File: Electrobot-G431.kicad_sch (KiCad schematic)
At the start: 53 parts, among them J1 Conn_XT30M, J10 Conn_01x03, J11 Conn_01x03, J12 Conn_01x04, J13 Conn_01x04, J14 Conn_01x04, J15 Conn_XT30F, J2 Conn_01x03, J3 Conn_01x03, J4 Conn_01x03, J5 Conn_01x04, J6 Conn_01x04, J7 Conn_XT30F, J8 Conn_XT30F, J9 Conn_01x03, Q1 BSP-76, U1 TSR_2-2450, U2 TSR_2-2465, U3 L293D

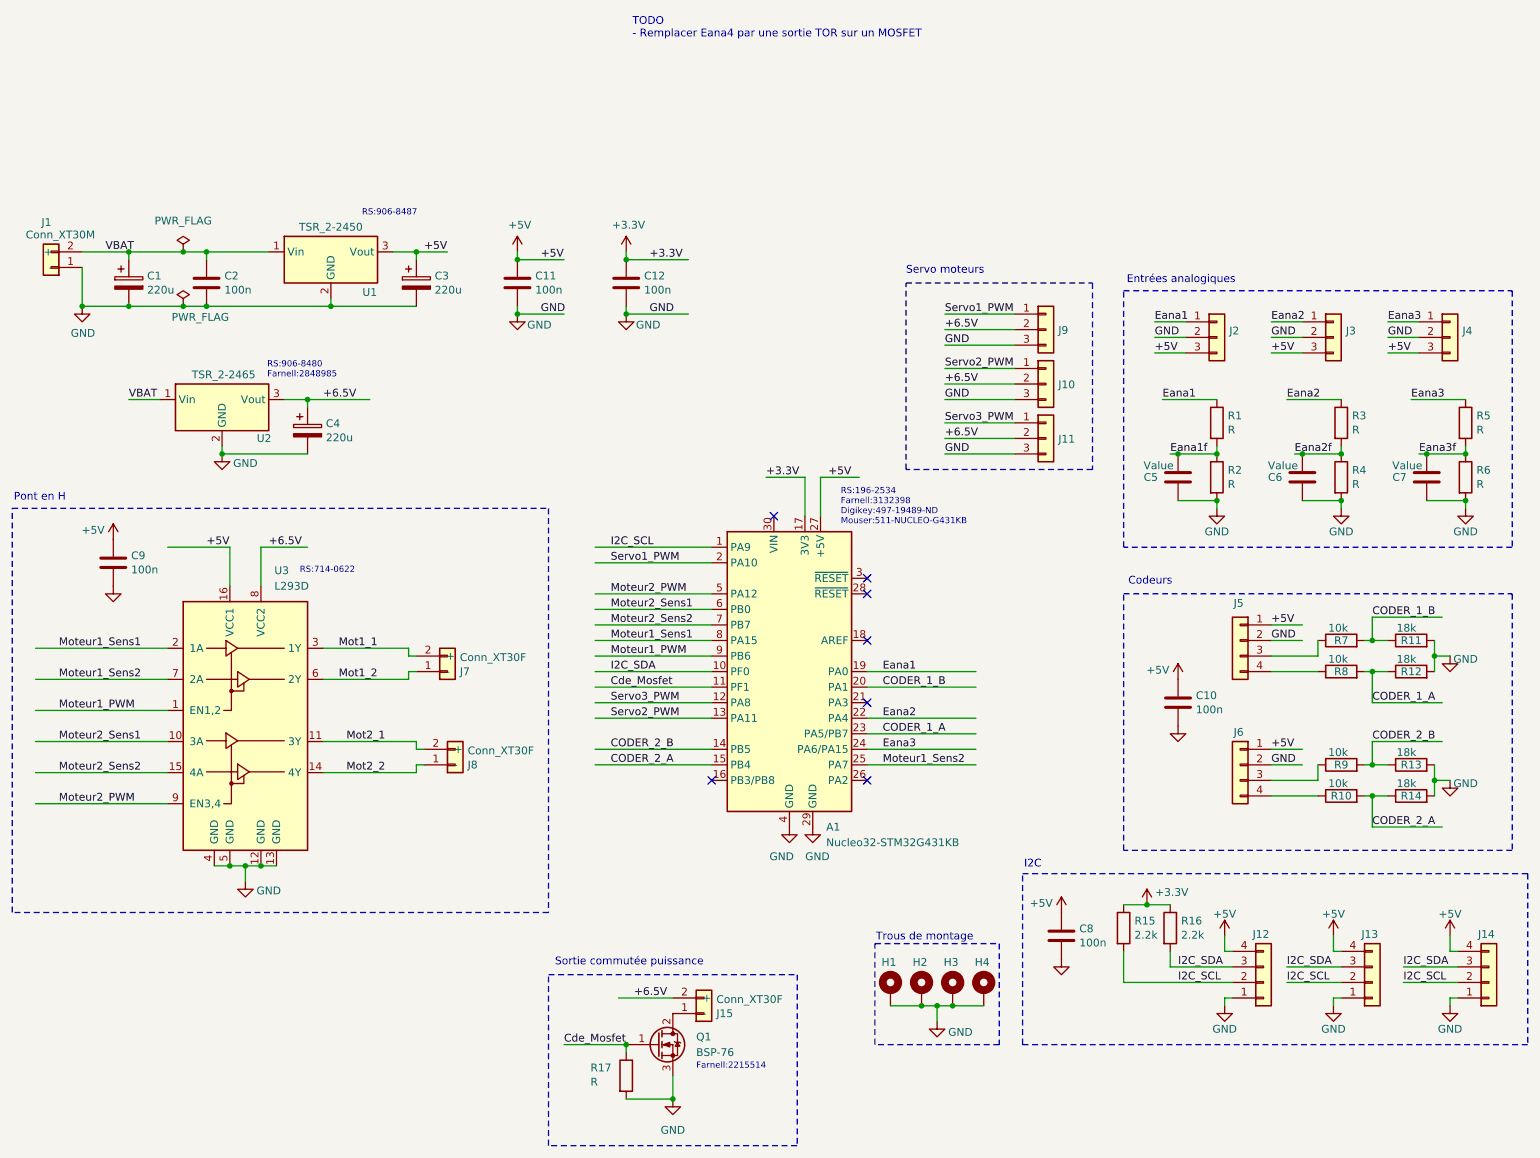
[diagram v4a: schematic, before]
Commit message: Mise à jour du schéma suite à la séance du 18/01/2025
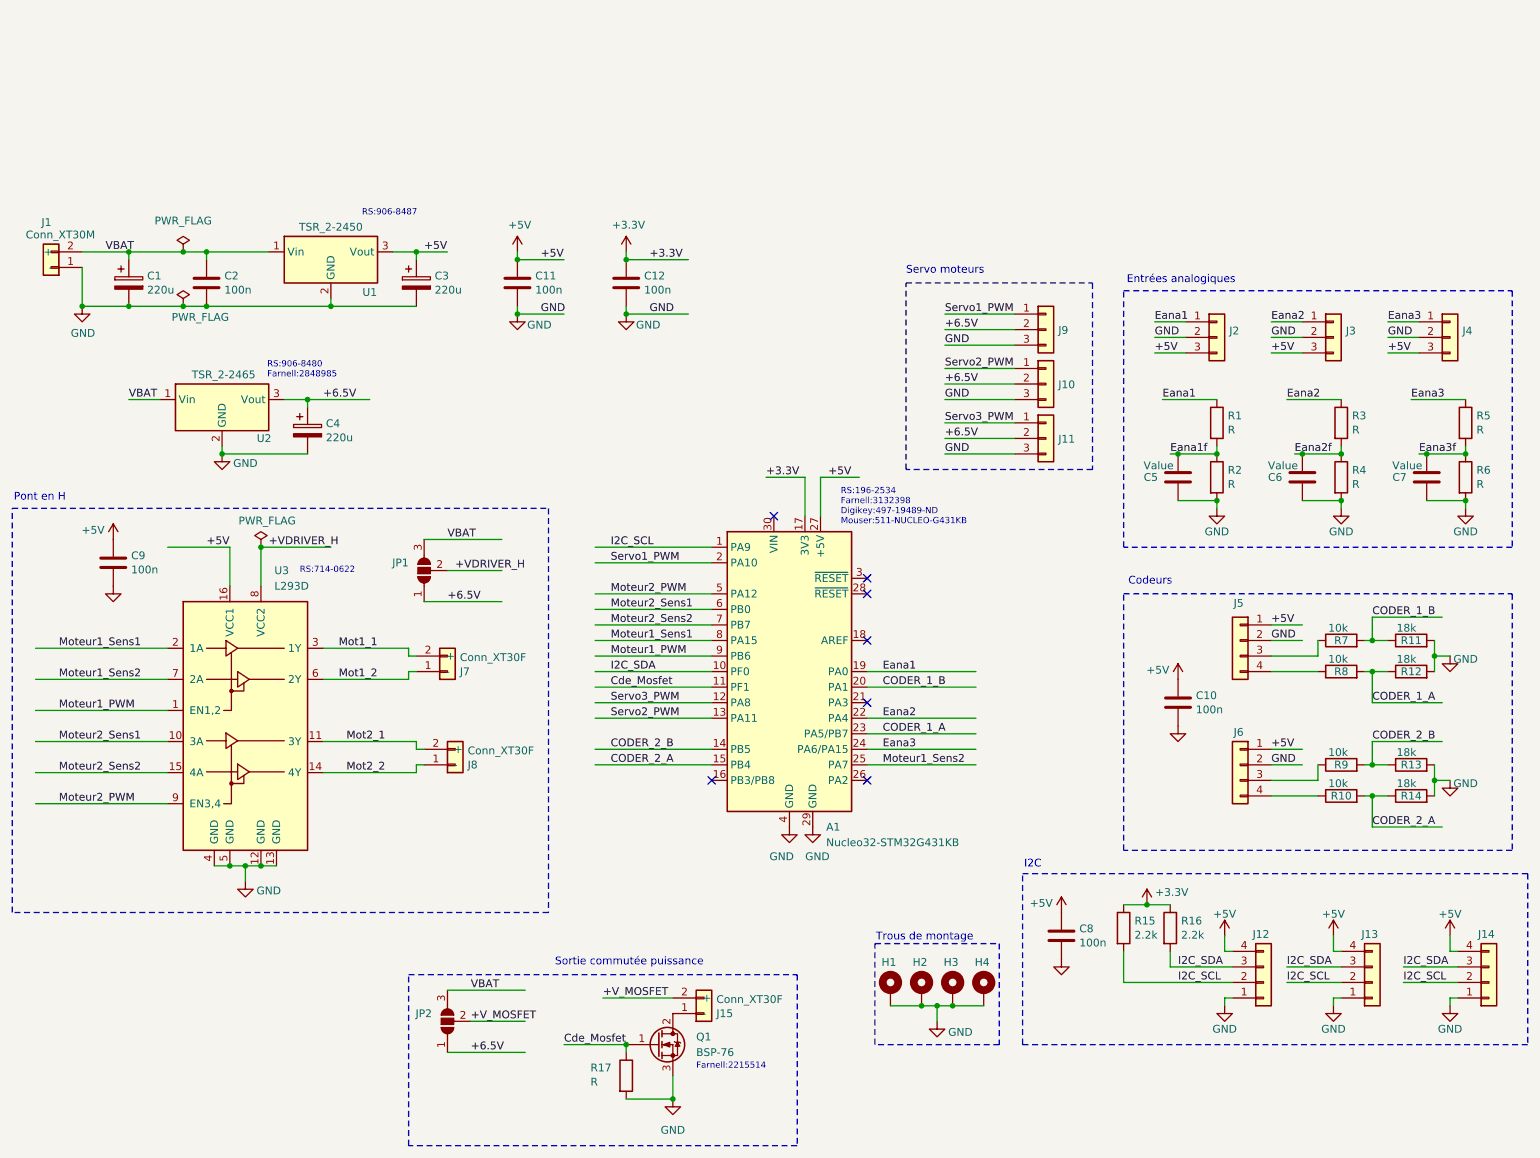
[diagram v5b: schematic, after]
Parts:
- added JP1, JP2: SolderJumper_3_Open, Connector_PinHeader_2.54mm:PinHeader_1x03_P2.54mm_Vertical, symbol Jumper:SolderJumper_3_Open
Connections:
- net +6.5V: now also JP1.1 (A), JP2.1 (A); no longer J15.2 (+), U3.8 (VCC2)
- net VBAT: now also JP1.3 (B), JP2.3 (B)
- new net +VDRIVER_H: JP1.2 (C), U3.8 (VCC2)
- new net +V_MOSFET: J15.2 (+), JP2.2 (C)
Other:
- note removed: "TODO - Remplacer Eana4 par une sortie TOR sur un MOSFET"

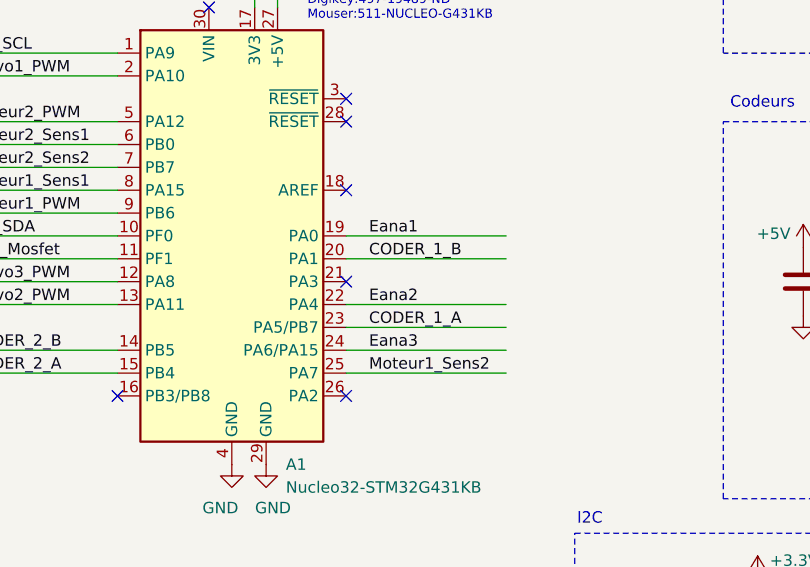
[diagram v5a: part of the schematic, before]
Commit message: Correction des entrées Eana1, Eana2, Eana3 -> Eana1f, Eana2f, Eana3f
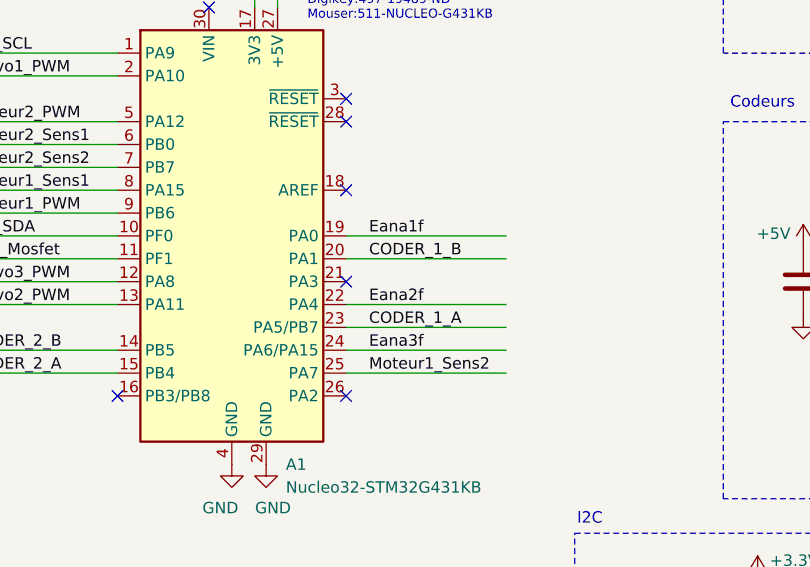
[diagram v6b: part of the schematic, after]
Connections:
- net Eana1: no longer A1.19 (PA0)
- net Eana1f: now also A1.19 (PA0)
- net Eana2: no longer A1.22 (PA4)
- net Eana2f: now also A1.22 (PA4)
- net Eana3: no longer A1.24 (PA6/PA15)
- net Eana3f: now also A1.24 (PA6/PA15)
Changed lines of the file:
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@@
 		)
 	)
-	(label "Eana1"
+	(label "Eana1f"
 		(at 156.21 88.9 0)
 		(fields_autoplaced yes)
@@
 		)
 	)
-	(label "Eana2"
+	(label "Eana2f"
 		(at 156.21 96.52 0)
 		(fields_autoplaced yes)
@@
 		)
 	)
-	(label "Eana3"
+	(label "Eana3f"
 		(at 156.21 101.6 0)
 		(fields_autoplaced yes)
